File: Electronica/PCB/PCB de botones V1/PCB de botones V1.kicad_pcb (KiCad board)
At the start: 2 copper layers, 14 parts, among them J1 Conn_02x05_Counter_Clockwise, SW1 SW_Push, SW2 SW_Push, SW3 SW_SPST

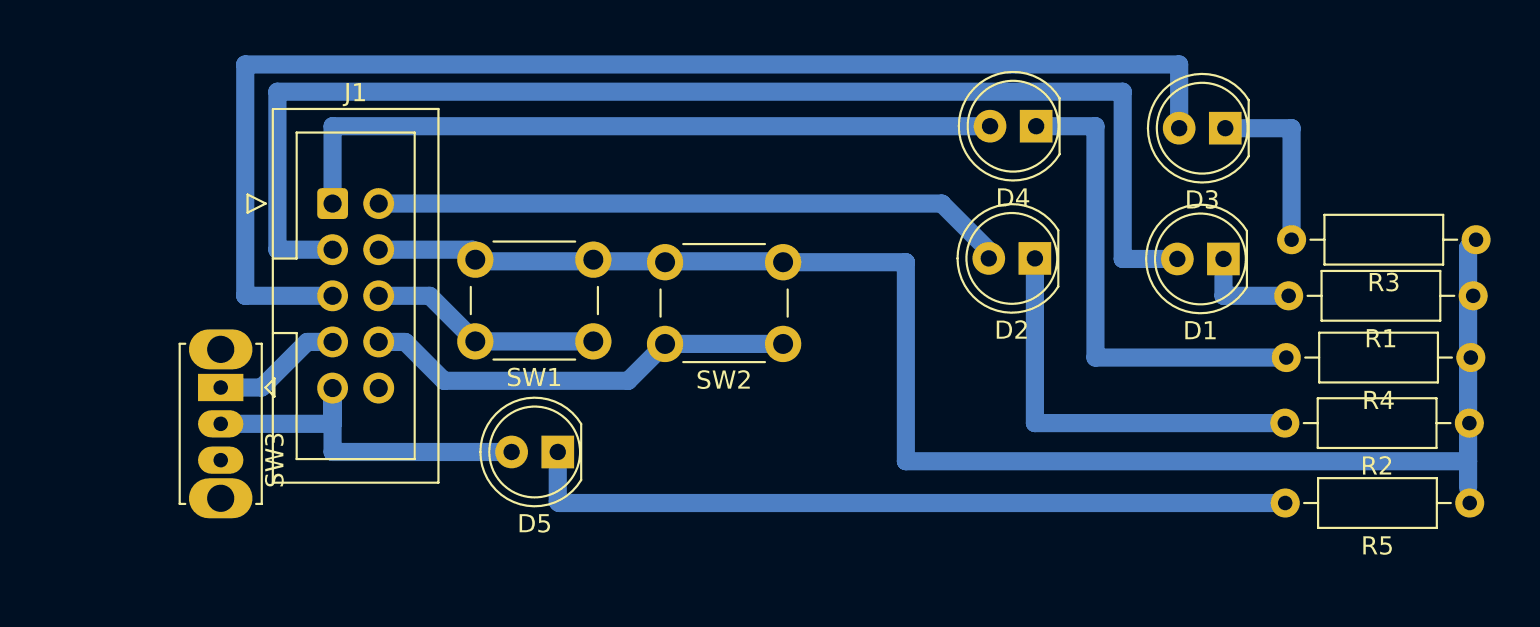
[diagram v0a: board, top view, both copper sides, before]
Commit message: Pcb botones con arreglos de distancias
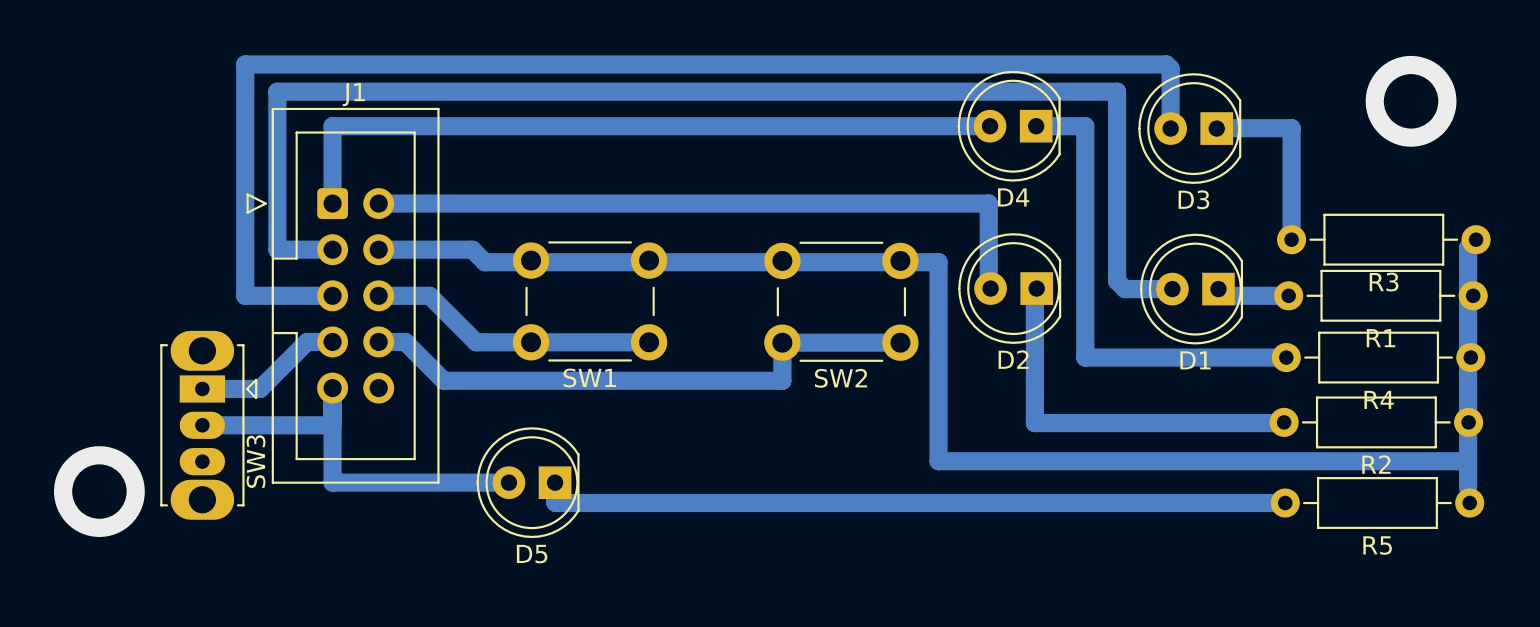
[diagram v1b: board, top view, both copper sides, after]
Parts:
- moved SW2 6.46 mm to (196.8, 89.3)
- moved SW1 3.07 mm to (183.0, 89.3)
- moved D5 1.70 mm to (177.8, 97.0)
- moved D1 1.68 mm to (214.3, 86.4)
- moved D2 1.66 mm to (204.3, 86.4)
- moved SW3 1.01 mm to (158.4, 91.9)
- moved D3 0.47 mm to (214.2, 77.5)
- moved R2 0.06 mm to (228.1, 93.7)
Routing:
- net Net-(J1-Pin_8): track 24.0 -> 31.7 mm
- net Net-(D2-A): track 35.1 -> 38.3 mm
- net Net-(J1-Pin_6): track 12.9 -> 16.0 mm
- net Net-(D5-A): track 21.5 -> 24.1 mm
- net Net-(D2-K): track 22.8 -> 21.1 mm
- net Net-(D5-K): track 43.0 -> 41.3 mm
- net Net-(D1-K): track 5.62 -> 4.06 mm
- net Net-(D1-A): track 70.5 -> 71.6 mm
- net Net-(J1-Pin_7): track 7.20 -> 8.24 mm
- net Net-(D3-A): track 72.5 -> 71.9 mm
- net (no net): vias 0 -> 2

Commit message: PCB de botones terminada
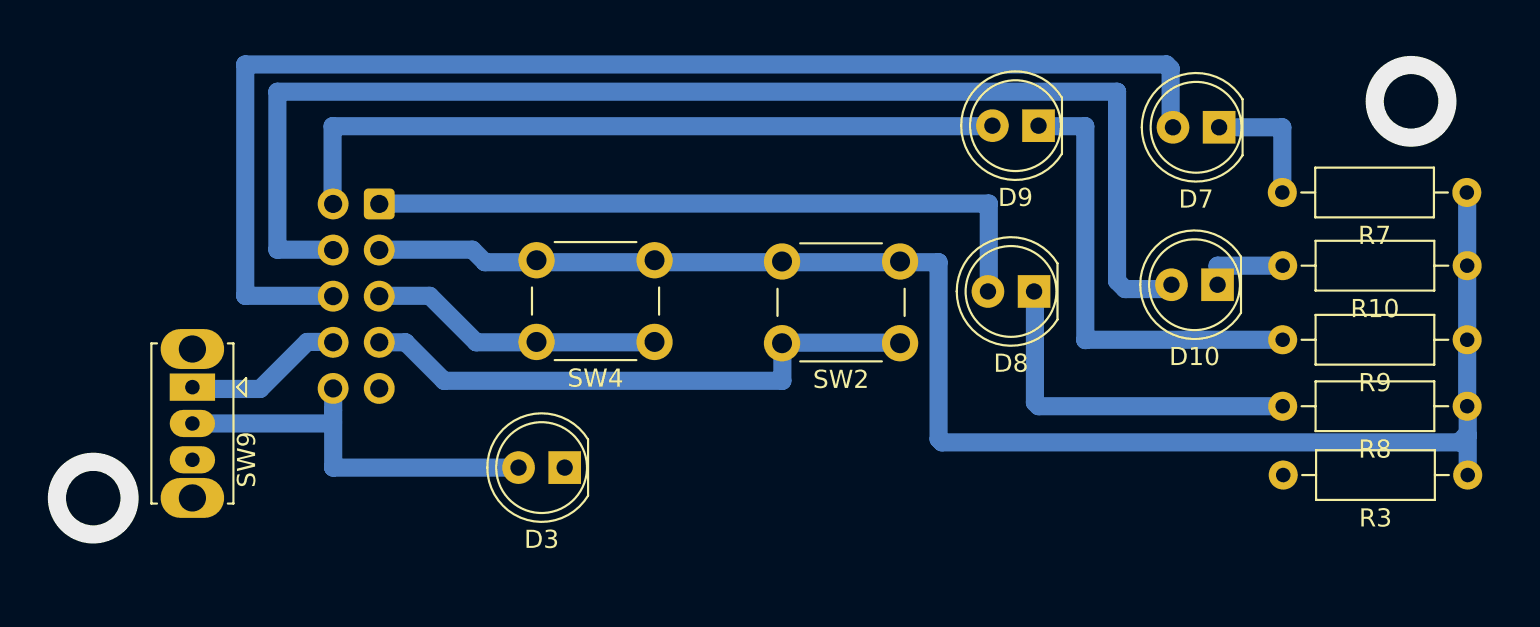
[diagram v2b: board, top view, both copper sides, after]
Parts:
- removed D1, D2, D4, D5: LED, LED_THT:LED_D5.0mm
- removed J1: Conn_02x05_Counter_Clockwise, Connector_IDC:IDC-Header_2x05_P2.54mm_Vertical
- removed R1, R2, R4, R5: R_US, Resistor_THT:R_Axial_DIN0207_L6.3mm_D2.5mm_P10.16mm_Horizontal
- removed SW1: SW_Push, Button_Switch_THT:SW_PUSH_6mm
- removed SW3: SW_SPST, Button_Switch_THT:SW_Slide_SPDT_Straight_CK_OS102011MS2Q
- added D10: LED, LED_THT:LED_D5.0mm, F.Cu at (214.3, 86.2)
- added D7: LED, LED_THT:LED_D5.0mm, F.Cu at (214.3, 77.5)
- added D8: LED, LED_THT:LED_D5.0mm, F.Cu at (204.2, 86.5)
- added D9: LED, LED_THT:LED_D5.0mm, F.Cu at (204.4, 77.4)
- added J2: Conn_02x05_Counter_Clockwise, Connector_IDC:IDC-Header_2x05_P2.54mm_Vertical, B.Cu at (168.1, 81.7)
- added R10: R_US, Resistor_THT:R_Axial_DIN0207_L6.3mm_D2.5mm_P10.16mm_Horizontal, F.Cu at (228.0, 85.1)
- added R7: R_US, Resistor_THT:R_Axial_DIN0207_L6.3mm_D2.5mm_P10.16mm_Horizontal, F.Cu at (228.0, 81.1)
- added R8: R_US, Resistor_THT:R_Axial_DIN0207_L6.3mm_D2.5mm_P10.16mm_Horizontal, F.Cu at (228.0, 92.8)
- added R9: R_US, Resistor_THT:R_Axial_DIN0207_L6.3mm_D2.5mm_P10.16mm_Horizontal, F.Cu at (228.0, 89.2)
- added SW4: SW_Push, Button_Switch_THT:SW_PUSH_6mm, F.Cu at (183.3, 89.3)
- added SW9: SW_SPST, Button_Switch_THT:SW_Slide_SPDT_Straight_CK_OS102011MS2Q, F.Cu at (157.8, 91.8)
- moved D3 40.5 mm to (178.3, 96.2)
- moved R3 13.0 mm to (228.0, 96.6)
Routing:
- net Net-(D7-A): track 0.00 -> 71.9 mm
- net Net-(D10-A): track 0.00 -> 71.6 mm
- net Net-(D1-A): track 71.6 -> 0.00 mm
- net Net-(D3-A): track 71.9 -> 22.3 mm
- net Net-(D5-K): track 41.3 -> 0.00 mm
- net Net-(D9-A): track 0.00 -> 40.5 mm
- net Net-(D4-A): track 40.5 -> 0.00 mm
- net Net-(D8-A): track 0.00 -> 38.3 mm
- net Net-(D2-A): track 38.3 -> 0.00 mm
- net Net-(D4-K): track 26.5 -> 0.00 mm
- net Net-(D9-K): track 0.00 -> 25.4 mm
- net Net-(D5-A): track 24.1 -> 0.00 mm
- net Net-(D2-K): track 21.1 -> 0.00 mm
- net Net-(D8-K): track 0.00 -> 19.9 mm
- net Net-(J2-Pin_5): track 0.00 -> 16.0 mm
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
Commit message: diseño terminado
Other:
- board outline added: 80.3 x 28.4 mm
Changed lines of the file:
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@@
 		(allow_soldermask_bridges_in_footprints no)
 		(pcbplotparams
-			(layerselection 0x00010fc_ffffffff)
-			(plot_on_all_layers_selection 0x0000000_00000000)
+			(layerselection 0x0000000_fffffffe)
+			(plot_on_all_layers_selection 0x0001000_00000000)
 			(disableapertmacros no)
 			(usegerberextensions no)
@@
 			(sketchpadsonfab no)
 			(subtractmaskfromsilk no)
-			(outputformat 1)
+			(outputformat 4)
 			(mirror no)
 			(drillshape 1)
 			(scaleselection 1)
-			(outputdirectory "")
+			(outputdirectory "../../../../../../Escritorio/")
 		)
 	)
@@
 		(end 229.92 100.93)
 		(stroke
-			(width 0.1)
+			(width 0.2)
 			(type default)
 		)
 		(fill none)
-		(layer "F.Adhes")
+		(layer "Edge.Cuts")
 	)
 	(via

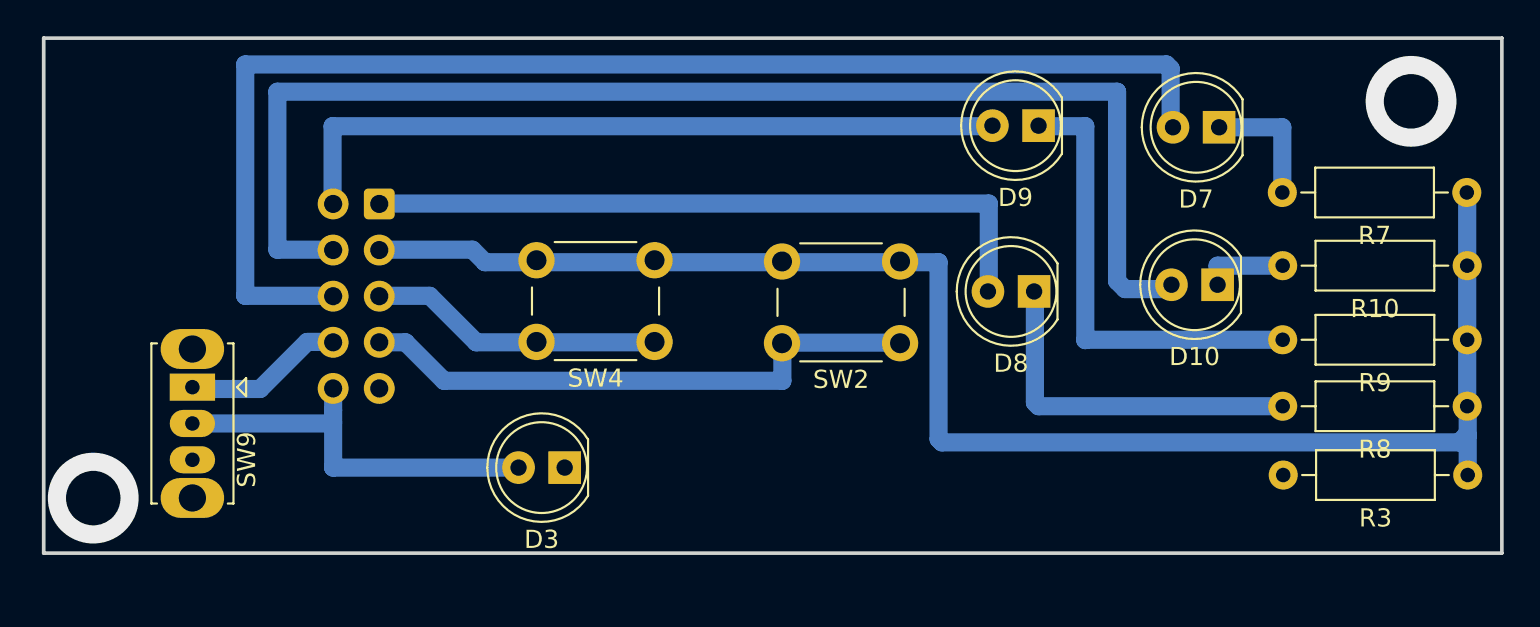
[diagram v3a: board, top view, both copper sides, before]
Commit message: vias pcb botones
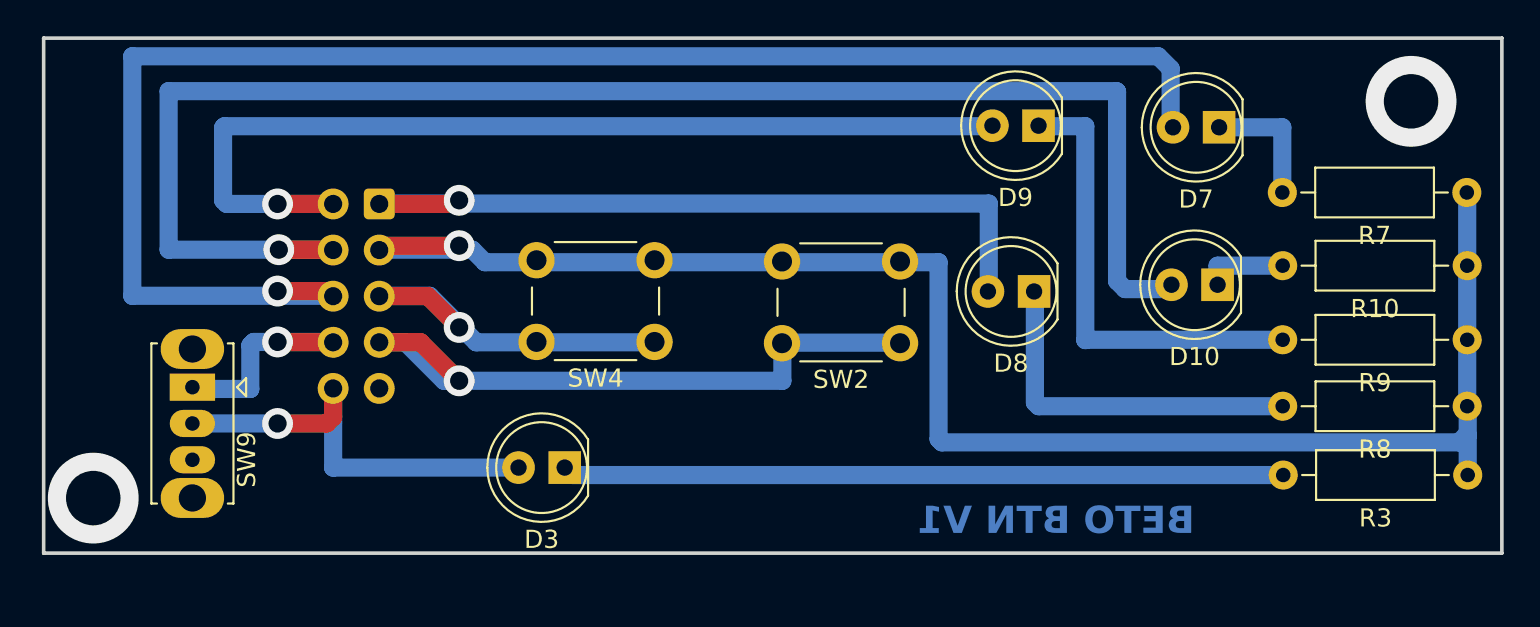
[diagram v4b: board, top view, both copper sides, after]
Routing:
- net Net-(D3-K): track 0.00 -> 39.7 mm
- net Net-(D7-A): track 71.9 -> 88.2 mm, vias 0 -> 1
- net Net-(D10-A): track 71.6 -> 86.7 mm, vias 0 -> 1
- net Net-(D9-A): track 40.5 -> 55.5 mm, vias 0 -> 1
- net Net-(J2-Pin_7): track 31.7 -> 37.0 mm, vias 0 -> 1
- net Net-(J2-Pin_5): track 16.0 -> 21.1 mm, vias 0 -> 1
- net Net-(D3-A): track 22.3 -> 27.1 mm, vias 0 -> 1
- net GND: track 85.8 -> 90.3 mm, vias 0 -> 1
- net Net-(D8-A): track 38.3 -> 42.8 mm, vias 0 -> 1
- net Net-(J2-Pin_8): track 8.24 -> 12.7 mm, vias 0 -> 1
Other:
- board text added: "BETO BTN V1"

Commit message: ?
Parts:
- D10, D3, D7, D8, D9, R10, R3, R7, R8, R9, SW2, SW4, SW9: moved to B.Cu
- J2: moved to F.Cu
- moved R3 76.9 mm to (151.2, 98.6), turned to 0 degrees
- moved R10 76.8 mm to (151.2, 87.1), turned to 0 degrees
- moved R8 76.8 mm to (151.2, 94.8), turned to 0 degrees
- moved R9 76.8 mm to (151.2, 91.2), turned to 0 degrees
- moved R7 76.8 mm to (151.2, 83.0), turned to 0 degrees
- moved SW9 63.6 mm to (221.4, 93.8)
- moved D7 49.5 mm to (164.9, 79.5), turned to 0 degrees
- moved D10 49.3 mm to (165.0, 88.1), turned to 0 degrees
- moved J2 43.1 mm to (211.1, 83.7), turned to 0 degrees
- moved D9 29.6 mm to (174.8, 79.4), turned to 0 degrees
- moved D8 29.2 mm to (175.1, 88.5), turned to 0 degrees
- moved D3 22.7 mm to (200.9, 98.2), turned to 0 degrees
- moved SW2 14.5 mm to (182.5, 91.3), turned to 0 degrees
- moved SW4 12.9 mm to (196.0, 91.3), turned to 0 degrees
